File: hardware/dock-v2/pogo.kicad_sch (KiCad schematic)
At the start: 15 parts, among them J601 Pogo 6-pin, Q601 2N7002, U601 TPD4E1U06DBVR, U602 SY6280AAC

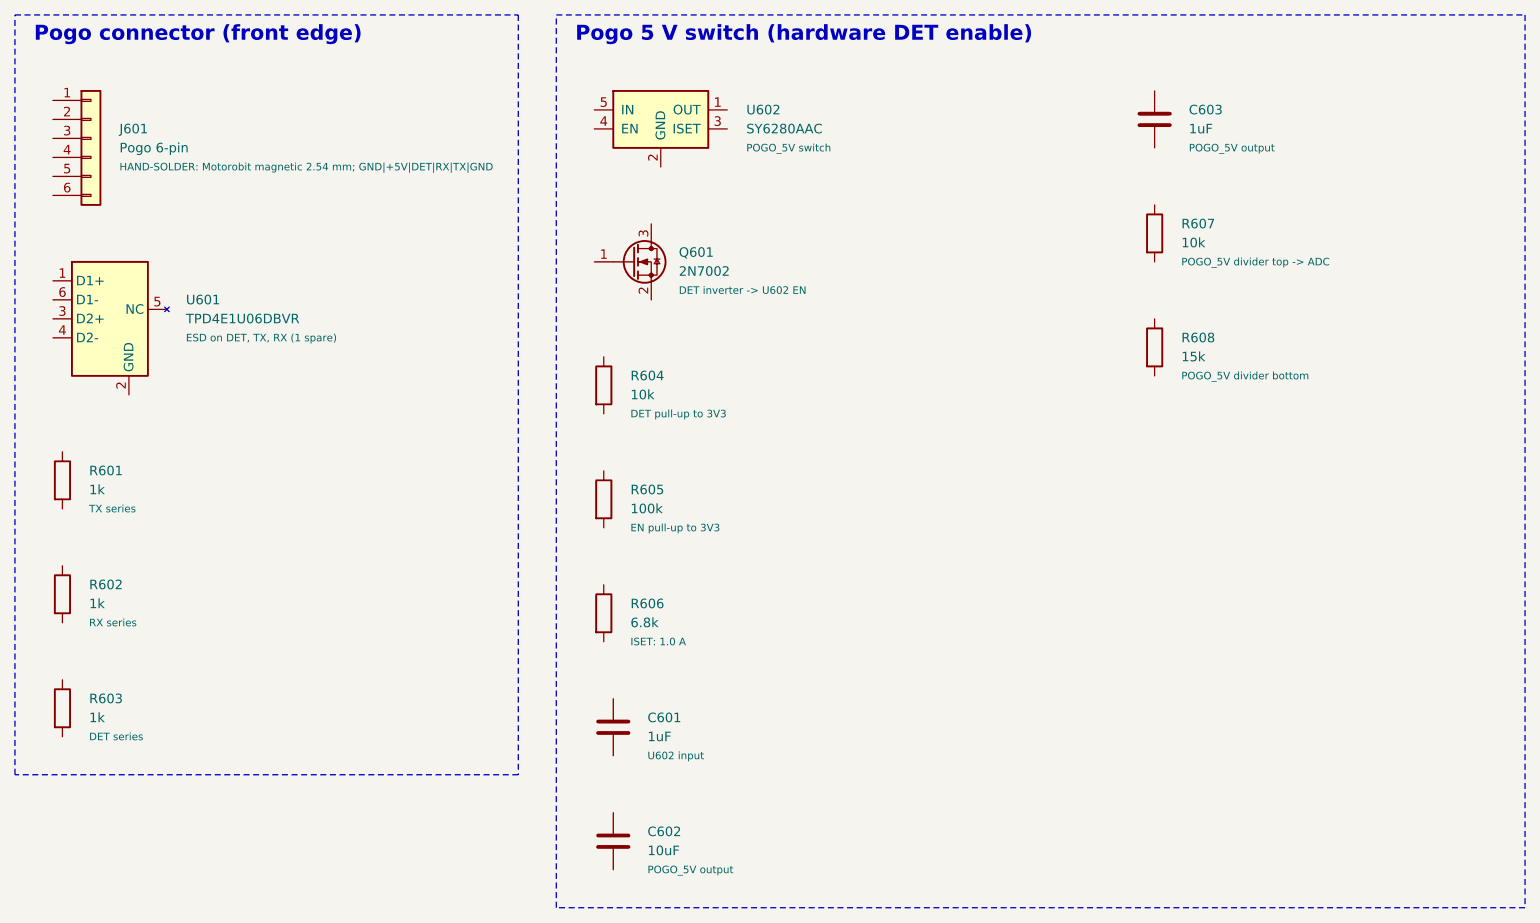
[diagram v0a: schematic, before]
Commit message: Dock v2 schematic fixes after review (J601 7-pin, Q602/R609, part data)
KiCad had the sheets open when the 7-pin pogo and the pull-up/veto parts were
added, and its save restored the old state. Restored now (KiCad closed):
- J601 -> Conn_01x07, footprint dock:Pogo-7; R606 4.7k (1.45 A)
- Q602 + R609 (POGO_OFF veto) added back to the pogo sheet
- L101 footprint L_TechFuse_SL0630 / LCSC C207841 again
- R406/R407 had the 1k LCSC number (copied from R405): now C25744; notes fixed
  on R406, R407, R504
- references back to the docs: C205->C107, R223->R106, R306->R201, R304->R202;
  R103/R104 swapped so R103 is on SCL and R104 on SDA (they were swapped, harmless)
- global label typo PD_SCA -> PD_SDA (both ends)
- net classes: 3V3_PWR, 5V_PWR (Power) and *USB_DP/*USB_DN/*USB_DM (USB),
  matching the labels used in the schematic

check_wiring.py: accepts interchangeable pins (R/C/button/crystal either way
round, TPD4E1U06 channels in any order), warns on a reversed L301/L401,
reports missing parts.

Co-Authored-By: Claude Opus 5.5 <noreply@anthropic.com>
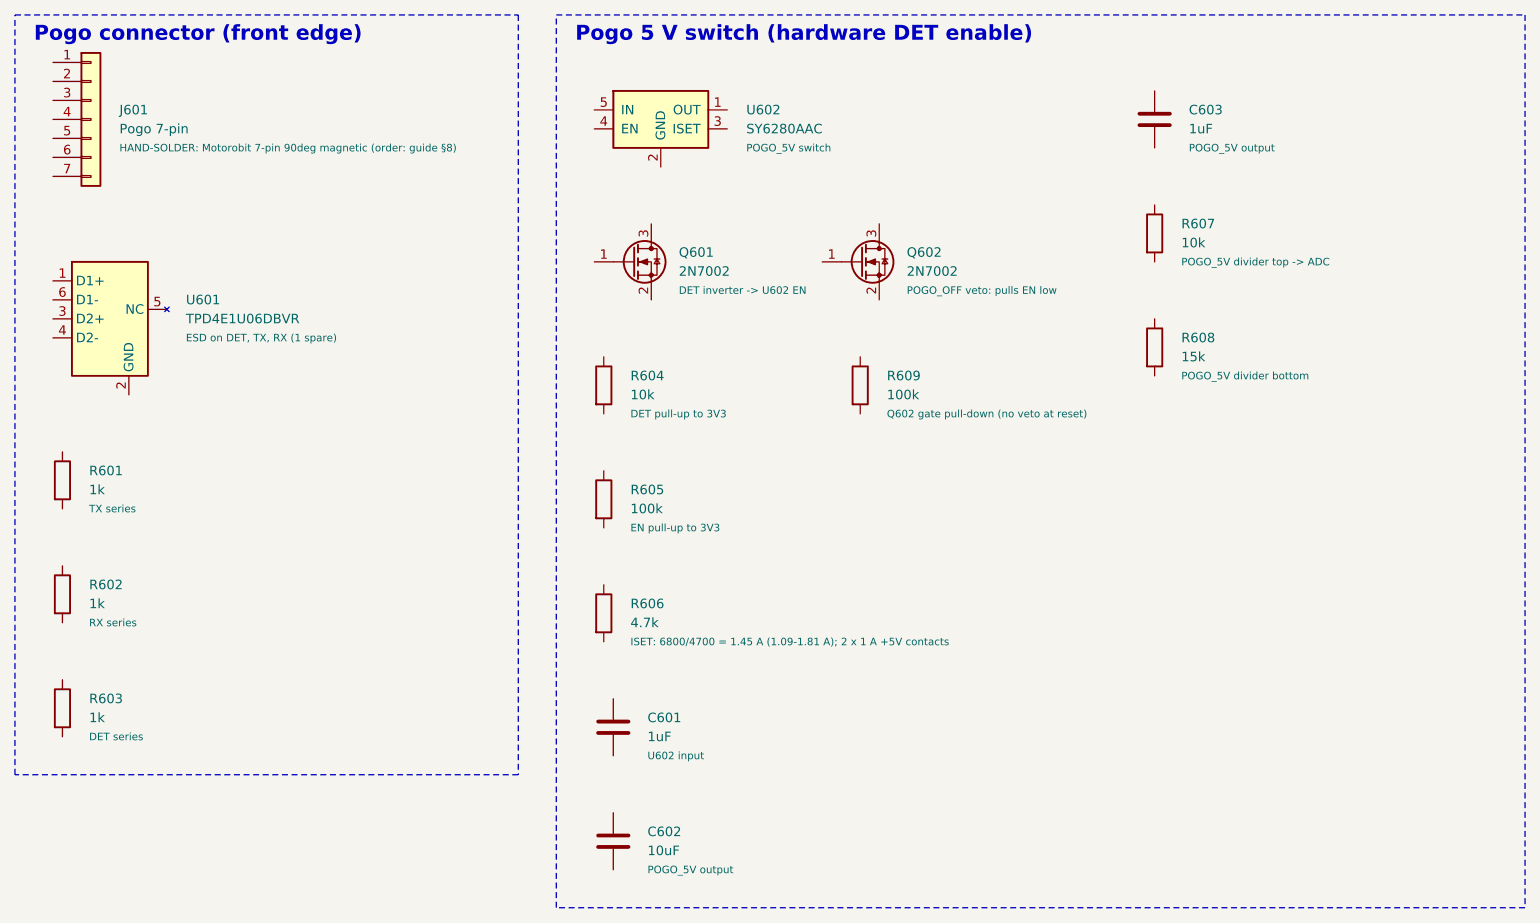
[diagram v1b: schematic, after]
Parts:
- added Q602: 2N7002, Package_TO_SOT_SMD:SOT-23, symbol Transistor_FET:2N7002
- added R609: 100k, Resistor_SMD:R_0402_1005Metric, symbol Device:R
- J601: value Pogo 6-pin -> Pogo 7-pin; footprint dock:Pogo-6 -> dock:Pogo-7; symbol Connector_Generic:Conn_01x06 -> Connector_Generic:Conn_01x07; Note HAND-SOLDER: Motorobit magnetic 2.54 mm; GND|+5V|DET|RX|TX|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 -> HAND-SOLDER: Motorobit 7-pin 90deg magnetic (order: guide §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
- R606: value 6.8k -> 4.7k; LCSC C25917 -> C25900; Note ISET: 1.0 A -> ISET: 6800/4700 = 1.45 A (1.09-1.81 A); 2 x 1 A +5V contacts
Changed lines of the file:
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@@
 			)
 		)
-		(property "Value" "6.8k"
+		(property "Value" "4.7k"
 			(at 95 99.06 0)
 			(show_name no)
@@
 			)
 		)
-		(property "LCSC" "C25917"
+		(property "LCSC" "C25900"
 			(at 91.44 97.79 0)
 			(hide yes)
@@
 			)
 		)
-		(property "Note" "ISET: 1.0 A"
+		(property "Note" "ISET: 6800/4700 = 1.45 A (1.09-1.81 A); 2 x 1 A +5V contacts"
 			(at 95 101.6 0)
 			(show_name no)
@@
 	)
 	(symbol
-		(lib_id "Connector_Generic:Conn_01x06")
-		(at 22.86 34.29 0)
+		(lib_id "Connector_Generic:Conn_01x07")
+		(at 22.86 31.75 0)
 		(unit 1)
 		(body_style 1)
@@
 		(dnp no)
 		(property "Reference" "J601"
+			(at 26.67 30.48 0)
+			(show_name no)
+			(do_not_autoplace no)
+			(effects
+				(font
+					(size 1.27 1.27)
+				)
+				(justify left)
+			)
+		)
+		(property "Value" "Pogo 7-pin"
 			(at 26.67 33.02 0)
 			(show_name no)
@@
 			)
 		)
-		(property "Value" "Pogo 6-pin"
+		(property "Footprint" "dock:Pogo-7"
+			(at 22.86 31.75 0)
+			(hide yes)
+			(show_name no)
+			(do_not_autoplace no)
+			(effects
+				(font
+					(size 1.27 1.27)
+				)
+			)
+		)
+		(property "Datasheet" ""
+			(at 22.86 31.75 0)
+			(hide yes)
+			(show_name no)
+			(do_not_autoplace no)
+			(effects
+				(font
+					(size 1.27 1.27)
+				)
+			)
+		)
+		(property "Description" "Generic connector, single row, 01x06, script generated (kicad-library-utils/schlib/autogen/connector/)"
+			(at 22.86 31.75 0)
+			(hide yes)
+			(show_name no)
+			(do_not_autoplace no)
+			(effects
+				(font
+					(size 1.27 1.27)
+				)
+			)
+		)
+		(property "LCSC" ""
+			(at 22.86 31.75 0)
+			(hide yes)
+			(show_name no)
+			(do_not_autoplace no)
+			(effects
+				(font
+					(size 1.27 1.27)
+				)
+			)
+		)
+		(property "Note" "HAND-SOLDER: Motorobit 7-pin 90deg magnetic (order: guide §8)"
 			(at 26.67 35.56 0)
 			(show_name no)
@@
 			(effects
 				(font
-					(size 1.27 1.27)
-				)
-				(justify left)
-			)
-		)
-		(property "Footprint" "dock:Pogo-6"
-			(at 22.86 34.29 0)
-			(hide yes)
-			(show_name no)
-			(do_not_autoplace no)
-			(effects
-				(font
-					(size 1.27 1.27)
-				)
-			)
-		)
-		(property "Datasheet" ""
-			(at 22.86 34.29 0)
-			(hide yes)
-			(show_name no)
-			(do_not_autoplace no)
-			(effects
-				(font
-					(size 1.27 1.27)
-				)
-			)
-		)
-		(property "Description" "Generic connector, single row, 01x06, script generated (kicad-library-utils/schlib/autogen/connector/)"
-			(at 22.86 34.29 0)
-			(hide yes)
-			(show_name no)
-			(do_not_autoplace no)
-			(effects
-				(font
-					(size 1.27 1.27)
-				)
-			)
-		)
-		(property "LCSC" ""
-			(at 22.86 34.29 0)
-			(hide yes)
-			(show_name no)
-			(do_not_autoplace no)
-			(effects
-				(font
-					(size 1.27 1.27)
-				)
-			)
-		)
-		(property "Note" "HAND-SOLDER: Motorobit magnetic 2.54 mm; GND|+5V|DET|RX|TX|GND"
-			(at 26.67 38.1 0)
-			(show_name no)
-			(do_not_autoplace no)
-			(effects
-				(font
 					(size 1 1)
 				)
@@
 		)
 		(pin "6"
+		)
+		(pin "7"
 		)
 		(instances
@@
 					(unit 1)
 				)
+			)
+		)
+	)
+	(symbol
+		(lib_id "Transistor_FET:2N7002")
+		(at 125.73 50.8 0)
+		(unit 1)
+		(body_style 1)
+		(exclude_from_sim no)
+		(in_bom yes)
+		(on_board yes)
+		(in_pos_files yes)
+		(dnp no)
+		(property "Reference" "Q602"
+			(at 131.95 49.53 0)
+			(show_name no)
+			(do_not_autoplace no)
+			(effects
+				(font
+					(size 1.27 1.27)
+				)
+				(justify left)
+			)
+		)
+		(property "Value" "2N7002"
+			(at 131.95 52.07 0)
+			(show_name no)
+			(do_not_autoplace no)
+			(effects
+				(font
+					(size 1.27 1.27)
+				)
+				(justify left)
+			)
+		)
+		(property "Footprint" "Package_TO_SOT_SMD:SOT-23"
+			(at 125.73 50.8 0)
+			(hide yes)
+			(show_name no)
+			(do_not_autoplace no)
+			(effects
+				(font
+					(size 1.27 1.27)
+				)
+			)
+		)
+		(property "Datasheet" "https://www.onsemi.com/pub/Collateral/NDS7002A-D.PDF"
+			(at 125.73 50.8 0)
+			(hide yes)
+			(show_name no)
+			(do_not_autoplace no)
+			(effects
+				(font
+					(size 1.27 1.27)
+				)
+			)
+		)
+		(property "Description" "0.115A Id, 60V Vds, N-Channel MOSFET, SOT-23"
+			(at 125.73 50.8 0)
+			(hide yes)
+			(show_name no)
+			(do_not_autoplace no)
+			(effects
+				(font
+					(size 1.27 1.27)
+				)
+			)
+		)
+		(property "LCSC" "C8545"
+			(at 125.73 50.8 0)
+			(hide yes)
+			(show_name no)
+			(do_not_autoplace no)
+			(effects
+				(font
+					(size 1.27 1.27)
+				)
+			)
+		)
+		(property "Note" "POGO_OFF veto: pulls EN low"
+			(at 131.95 54.61 0)
+			(show_name no)
+			(do_not_autoplace no)
+			(effects
+				(font
+					(size 1 1)
+				)
+				(justify left)
+			)
+		)
+		(pin "1"
+		)
+		(pin "2"
+		)
+		(pin "3"
+		)
+		(instances
+			(project "dock-v2"
+				(path "/928a9dc6-b0ce-4f47-a17d-f26fd77e396a/a6551cad-76cb-43b5-b19c-441e3fa27a27"
+					(reference "Q602")
+					(unit 1)
+				)
+			)
+		)
+	)
+	(symbol
+		(lib_id "Device:R")
+		(at 125.73 67.31 0)
+		(unit 1)
+		(body_style 1)
+		(exclude_from_sim no)
+		(in_bom yes)
+		(on_board yes)
+		(in_pos_files yes)
+		(dnp no)
+		(property "Reference" "R609"
+			(at 129.29 66.04 0)
+			(show_name no)
+			(do_not_autoplace no)
+			(effects
+				(font
+					(size 1.27 1.27)
+				)
+				(justify left)
+			)
+		)
+		(property "Value" "100k"
+			(at 129.29 68.58 0)
+			(show_name no)
+			(do_not_autoplace no)
+			(effects
+				(font
+					(size 1.27 1.27)
+				)
+				(justify left)
+			)
+		)
+		(property "Footprint" "Resistor_SMD:R_0402_1005Metric"
+			(at 125.73 67.31 0)
+			(hide yes)
+			(show_name no)
+			(do_not_autoplace no)
+			(effects
+				(font
+					(size 1.27 1.27)
+				)
+			)
+		)
+		(property "Datasheet" ""
+			(at 125.73 67.31 0)
+			(hide yes)
+			(show_name no)
+			(do_not_autoplace no)
+			(effects
+				(font
+					(size 1.27 1.27)
+				)
+			)
+		)
+		(property "Description" "Resistor"
+			(at 125.73 67.31 0)
+			(hide yes)
+			(show_name no)
+			(do_not_autoplace no)
+			(effects
+				(font
+					(size 1.27 1.27)
+				)
+			)
+		)
+		(property "LCSC" "C25741"
+			(at 125.73 67.31 0)
+			(hide yes)
+			(show_name no)
+			(do_not_autoplace no)
+			(effects
+				(font
+					(size 1.27 1.27)
+				)
+			)
+		)
+		(property "Note" "Q602 gate pull-down (no veto at reset)"
+			(at 129.29 71.12 0)
+			(show_name no)
+			(do_not_autoplace no)
+			(effects
+				(font
+					(size 1 1)
+				)
+				(justify left)
+			)
+		)
+		(pin "1"
+		)
+		(pin "2"
+		)
+		(instances
+			(project "dock-v2"
+				(path "/928a9dc6-b0ce-4f47-a17d-f26fd77e396a/a6551cad-76cb-43b5-b19c-441e3fa27a27"
+					(reference "R609")
+					(unit 1)
+				)
